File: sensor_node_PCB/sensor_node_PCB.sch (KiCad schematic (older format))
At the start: 1 part

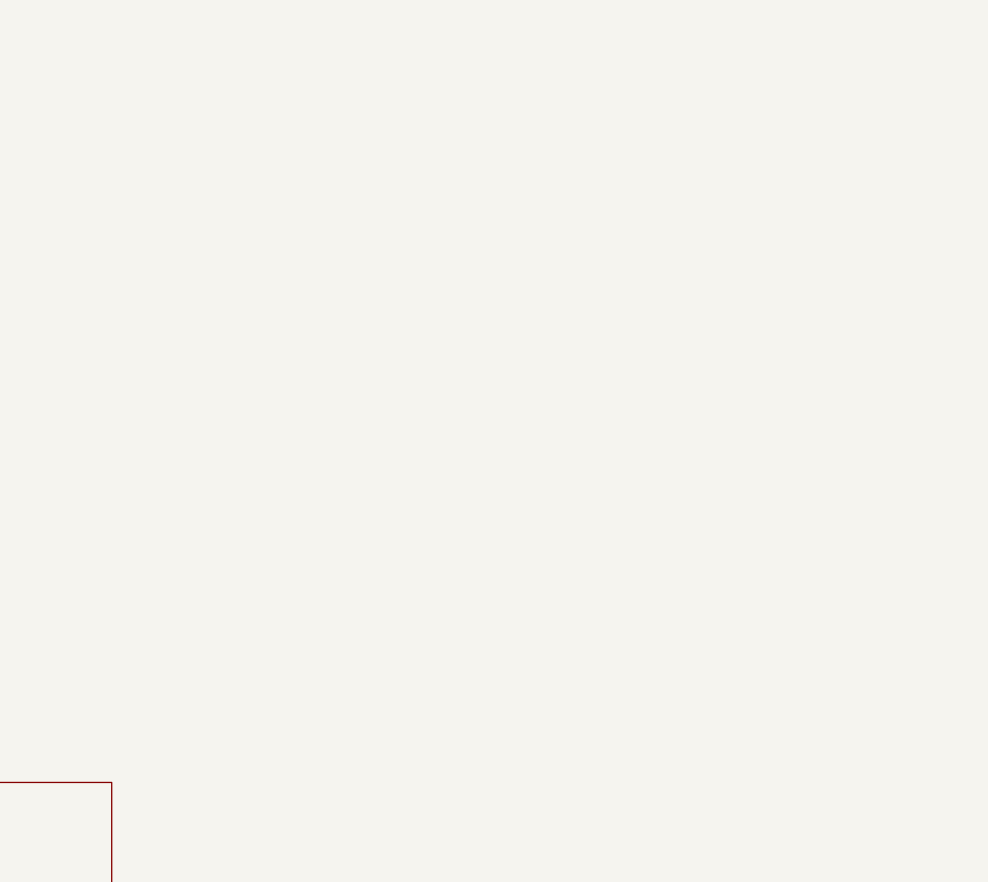
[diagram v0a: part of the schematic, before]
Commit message: added modbus connectors
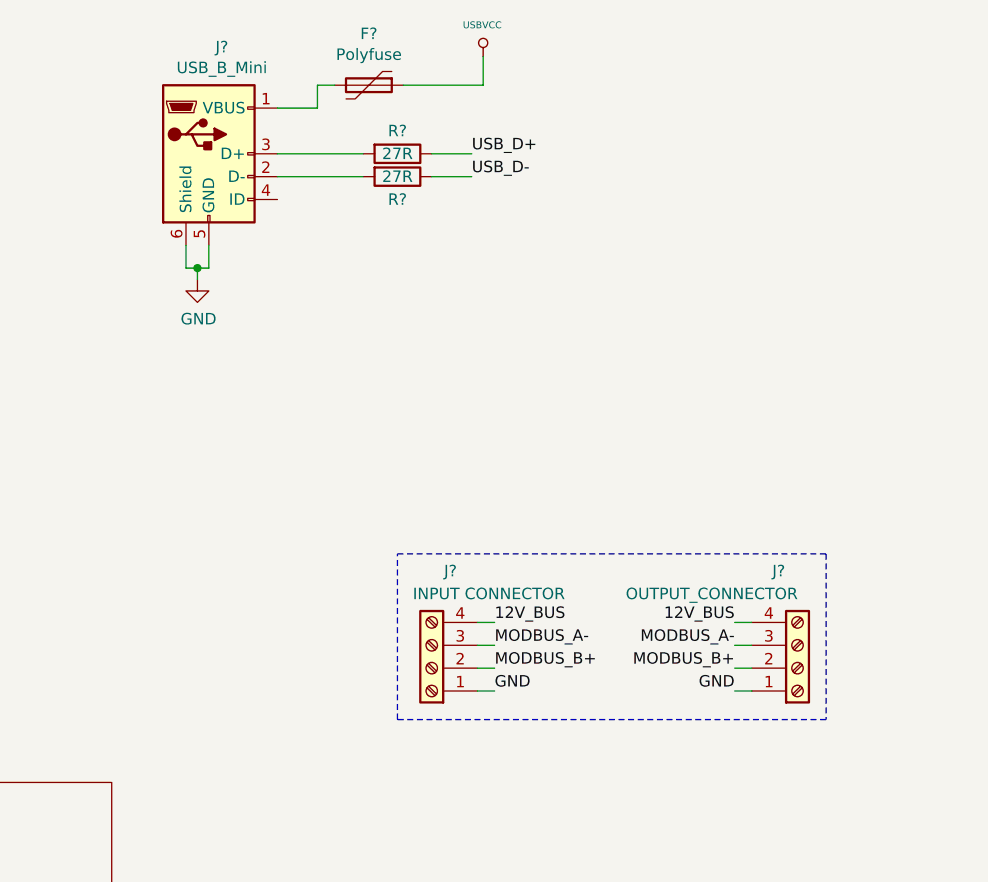
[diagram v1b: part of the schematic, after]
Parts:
- added F?: Polyfuse, symbol Device:Polyfuse
- added J?: USB_B_Mini, symbol Connector:USB_B_Mini
- added J?: INPUT CONNECTOR, symbol Connector:Screw_Terminal_01x04
- added J?: OUTPUT_CONNECTOR, symbol Connector:Screw_Terminal_01x04
- added R? (x2): 27R, symbol Arduino_Uno_R3_From_Scratch-rescue:R
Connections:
- new net: F?.2, J?.1 (VBUS)
- new net: J?.2 (D-), R?.2
- new net: J?.3 (D+), R?.2
- new net 12V_BUS: J?.4 (Pin_4), J?.4 (Pin_4)
- new net GND: J?.1 (Pin_1), J?.1 (Pin_1), J?.5 (GND), J?.6 (Shield)
- new net MODBUS_A-: J?.3 (Pin_3), J?.3 (Pin_3)
- new net MODBUS_B+: J?.2 (Pin_2), J?.2 (Pin_2)
- new net USBVCC: F?.1
- new net USB_D+: R?.1
- new net USB_D-: R?.1
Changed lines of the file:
@@
 F1 "voltage_regulator.sch" 50
 $EndSheet
+$Comp
+L Connector:USB_B_Mini J?
+U 1 1 5F4E1AA5
+P 3775 1200
+F 0 "J?" H 3832 1667 50  0000 C CNN
+F 1 "USB_B_Mini" H 3832 1576 50  0000 C CNN
+F 2 "" H 3925 1150 50  0001 C CNN
+F 3 "~" H 3925 1150 50  0001 C CNN
+	1    3775 1200
+	1    0    0    -1
+$EndComp
+$Comp
+L Arduino_Uno_R3_From_Scratch-rescue:R R?
+U 1 1 5F4E3CCC
+P 4600 1200
+F 0 "R?" V 4500 1200 50  0000 C CNN
+F 1 "27R" V 4600 1200 50  0000 C CNN
+F 2 "" V 4530 1200 30  0000 C CNN
+F 3 "" H 4600 1200 30  0000 C CNN
+	1    4600 1200
+	0    1    1    0
+$EndComp
+$Comp
+L Arduino_Uno_R3_From_Scratch-rescue:R R?
+U 1 1 5F4E5156
+P 4600 1300
+F 0 "R?" V 4700 1300 50  0000 C CNN
+F 1 "27R" V 4600 1300 50  0000 C CNN
+F 2 "" V 4530 1300 30  0000 C CNN
+F 3 "" H 4600 1300 30  0000 C CNN
+	1    4600 1300
+	0    1    1    0
+$EndComp
+$Comp
+L Device:Polyfuse F?
+U 1 1 5F4E6403
+P 4475 900
+F 0 "F?" V 4250 900 50  0000 C CNN
+F 1 "Polyfuse" V 4341 900 50  0000 C CNN
+F 2 "" H 4525 700 50  0001 L CNN
+F 3 "~" H 4475 900 50  0001 C CNN
+	1    4475 900
+	0    1    1    0
+$EndComp
+Wire Wire Line
+	4075 1000 4250 1000
+Wire Wire Line
+	4250 1000 4250 900
+Wire Wire Line
+	4250 900  4325 900
+$Comp
+L Arduino_Uno_R3_From_Scratch-rescue:USBVCC #PWR?
+U 1 1 5F4E7EA2
+P 4975 775
+F 0 "#PWR?" H 4975 865 20  0001 C CNN
+F 1 "USBVCC" H 4971 913 30  0000 C CNN
+F 2 "" H 4975 775 60  0000 C CNN
+F 3 "" H 4975 775 60  0000 C CNN
+	1    4975 775
+	1    0    0    -1
+$EndComp
+Wire Wire Line
+	4975 900  4975 775
+Wire Wire Line
+	4625 900  4975 900
+Wire Wire Line
+	4075 1200 4450 1200
+Wire Wire Line
+	4075 1300 4450 1300
+Wire Wire Line
+	4750 1200 4925 1200
+Wire Wire Line
+	4750 1300 4925 1300
+Text Label 4925 1200 0    50   ~ 0
+USB_D+
+Text Label 4925 1300 0    50   ~ 0
+USB_D-
+$Comp
+L Arduino_Uno_R3_From_Scratch-rescue:GND #PWR?
+U 1 1 5F4E97D5
+P 3725 1750
+F 0 "#PWR?" H 3725 1500 50  0001 C CNN
+F 1 "GND" H 3730 1577 50  0000 C CNN
+F 2 "" H 3725 1750 60  0000 C CNN
+F 3 "" H 3725 1750 60  0000 C CNN
+	1    3725 1750
+	1    0    0    -1
+$EndComp
+Wire Wire Line
+	3675 1600 3675 1700
+Wire Wire Line
+	3675 1700 3725 1700
+Wire Wire Line
+	3725 1700 3725 1750
+Wire Wire Line
+	3775 1600 3775 1700
+Wire Wire Line
+	3775 1700 3725 1700
+Connection ~ 3725 1700
+$Comp
+L Connector:Screw_Terminal_01x04 J?
+U 1 1 5F4EDCB8
+P 4750 3450
+F 0 "J?" H 4668 3025 50  0000 C CNN
+F 1 "INPUT CONNECTOR" H 4500 3125 50  0000 C CNN
+F 2 "" H 4750 3450 50  0001 C CNN
+F 3 "~" H 4750 3450 50  0001 C CNN
+	1    4750 3450
+	-1   0    0    1
+$EndComp
+$Comp
+L Connector:Screw_Terminal_01x04 J?
+U 1 1 5F4EE65B
+P 6350 3450
+F 0 "J?" H 6268 3025 50  0000 C CNN
+F 1 "OUTPUT_CONNECTOR" H 5975 3125 50  0000 C CNN
+F 2 "" H 6350 3450 50  0001 C CNN
+F 3 "~" H 6350 3450 50  0001 C CNN
+	1    6350 3450
+	1    0    0    1
+$EndComp
+Text Label 5025 3250 0    50   ~ 0
+12V_BUS
+Text Label 5025 3450 0    50   ~ 0
+MODBUS_B+
+Text Label 5025 3350 0    50   ~ 0
+MODBUS_A-
+Text Label 5025 3550 0    50   ~ 0
+GND
+Text Label 6075 3250 2    50   ~ 0
+12V_BUS
+Text Label 6075 3350 2    50   ~ 0
+MODBUS_A-
+Text Label 6075 3450 2    50   ~ 0
+MODBUS_B+
+Text Label 6075 3550 2    50   ~ 0
+GND
+Wire Notes Line
+	4600 2950 6475 2950
+Wire Notes Line
+	6475 2950 6475 3675
+Wire Notes Line
+	6475 3675 4600 3675
+Wire Notes Line
+	4600 3675 4600 2950
+Wire Wire Line
+	4950 3250 5025 3250
+Wire Wire Line
+	4950 3350 5025 3350
+Wire Wire Line
+	4950 3450 5025 3450
+Wire Wire Line
+	4950 3550 5025 3550
+Wire Wire Line
+	6075 3250 6150 3250
+Wire Wire Line
+	6075 3350 6150 3350
+Wire Wire Line
+	6075 3450 6150 3450
+Wire Wire Line
+	6075 3550 6150 3550
 $EndSCHEMATC

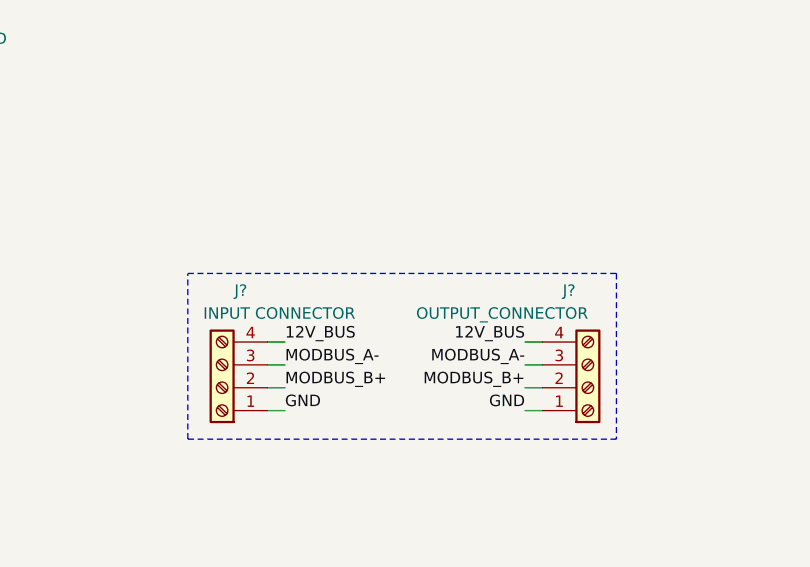
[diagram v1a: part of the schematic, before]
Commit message: changed 12v input to global label
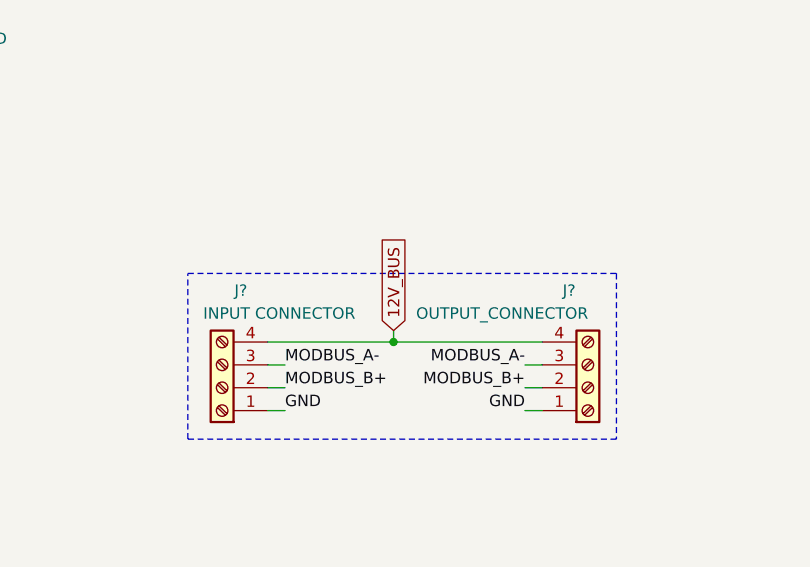
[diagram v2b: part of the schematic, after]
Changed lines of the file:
@@
 	1    0    0    1
 $EndComp
-Text Label 5025 3250 0    50   ~ 0
-12V_BUS
 Text Label 5025 3450 0    50   ~ 0
 MODBUS_B+
@@
 Text Label 5025 3550 0    50   ~ 0
 GND
-Text Label 6075 3250 2    50   ~ 0
-12V_BUS
 Text Label 6075 3350 2    50   ~ 0
 MODBUS_A-
@@
 	4600 3675 4600 2950
 Wire Wire Line
-	4950 3250 5025 3250
-Wire Wire Line
 	4950 3350 5025 3350
 Wire Wire Line
@@
 	4950 3550 5025 3550
 Wire Wire Line
-	6075 3250 6150 3250
-Wire Wire Line
 	6075 3350 6150 3350
 Wire Wire Line
@@
 Wire Wire Line
 	6075 3550 6150 3550
+Text GLabel 5500 3200 1    50   Input ~ 0
+12V_BUS
+Wire Wire Line
+	4950 3250 5500 3250
+Wire Wire Line
+	5500 3250 5500 3200
+Connection ~ 5500 3250
+Wire Wire Line
+	5500 3250 6150 3250
 $EndSCHEMATC

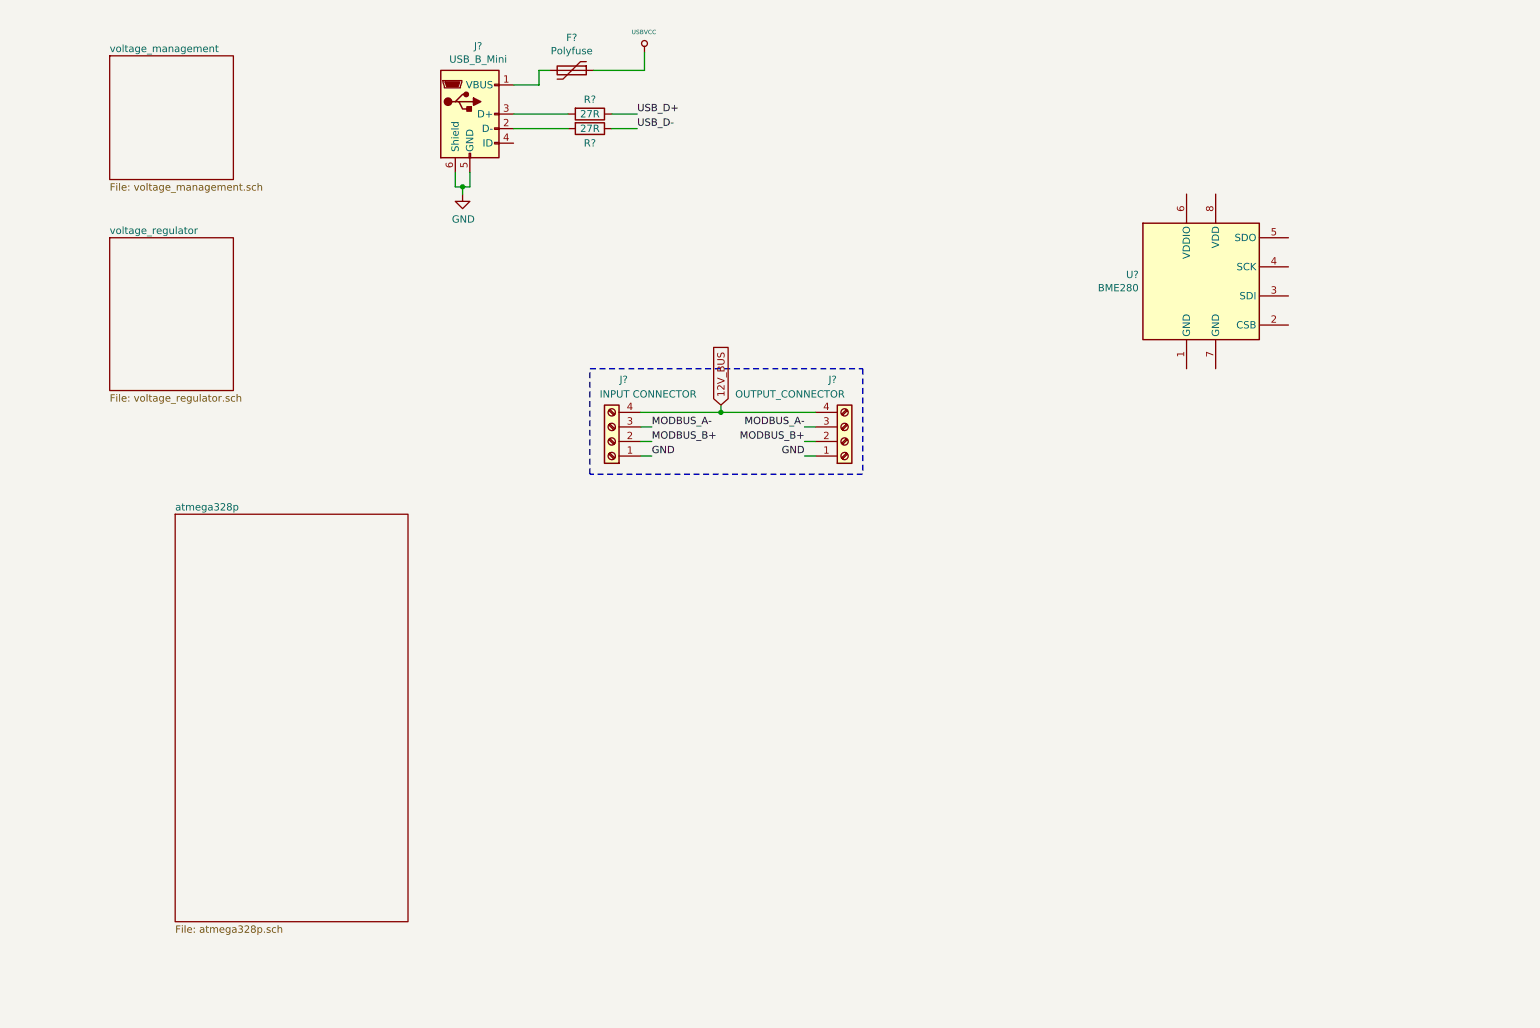
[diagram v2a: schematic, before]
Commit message: added 3.3v regulator
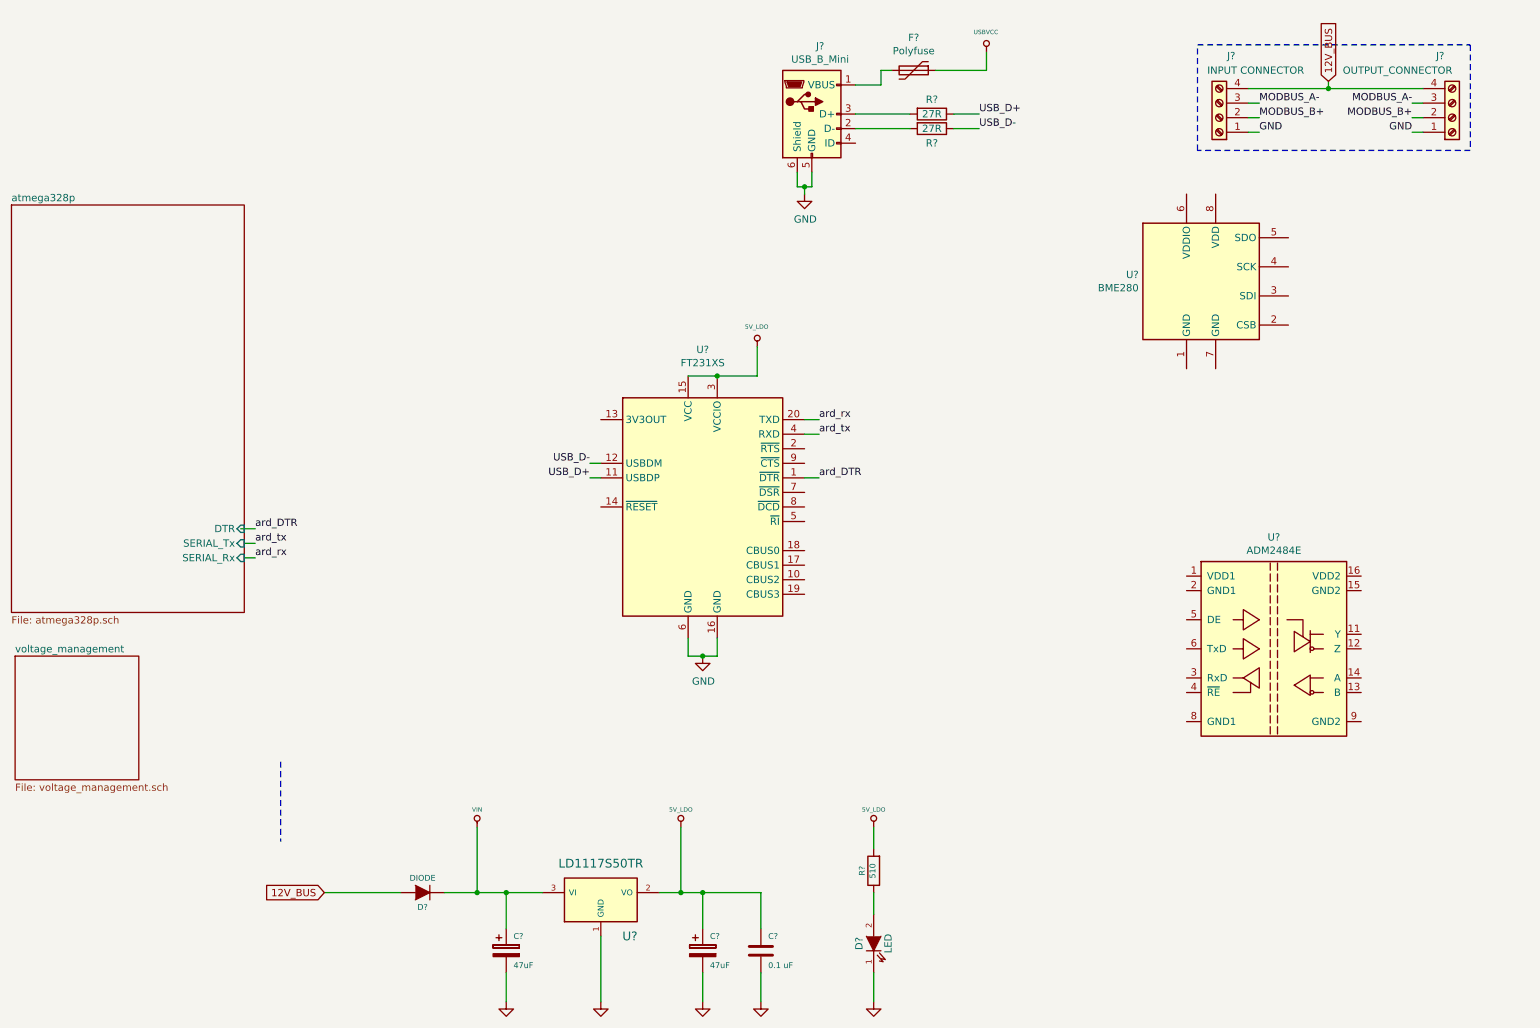
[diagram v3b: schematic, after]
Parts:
- added C? (x2): 47uF, ~, symbol Arduino_Uno_R3_From_Scratch-rescue:CP
- added C?: 0.1 uF, ~, symbol Arduino_Uno_R3_From_Scratch-rescue:C
- added D?: DIODE, ~, symbol Arduino_Uno_R3_From_Scratch-rescue:D
- added D?: LED, ~, symbol Arduino_Uno_R3_From_Scratch-rescue:LED
- added R?: 510, ~, symbol Arduino_Uno_R3_From_Scratch-rescue:R
- added U?: FT231XS, Package_SO:SSOP-20_3.9x8.7mm_P0.635mm, symbol Interface_USB:FT231XS
- added U?: ADM2484E, Package_SO:SOIC-16W_7.5x10.3mm_P1.27mm, symbol Interface_UART:ADM2484E
- added U?: LD1117S50TR, symbol Arduino_Uno_R3_From_Scratch-rescue:LD1117S50TR
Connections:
- net 12V_BUS: now also D?.2 (A)
- net GND: now also C?.2, C?.2, C?.2, D?.1 (K), U?.1 (GND), U?.16 (GND), U?.6 (GND)
- net USB_D+: now also U?.11 (USBDP)
- net USB_D-: now also U?.12 (USBDM)
- new net: D?.2 (A), R?.1
- new net 5V_LDO: C?.1, C?.1, R?.2, U?.15 (VCC), U?.2 (VO), U?.3 (VCCIO)
- new net Vin: C?.1, D?.1 (K), U?.3 (VI)
- new net ard_DTR: U?.1 (~DTR)
- new net ard_rx: U?.20 (TXD)
- new net ard_tx: U?.4 (RXD)
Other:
- moved on the sheet: F?, J?, R?
